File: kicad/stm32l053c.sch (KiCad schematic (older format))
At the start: 13 parts, among them P1 SWD, U1 STM32L053C8_LQFP48

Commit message: LCD footprint
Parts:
- added U1: LCD_KITCHEN_TIMER, symbol LCD_KITCHEN_TIMER
- gave numbers to parts that had none: 1
- renumbered C5 to C1, C7 to C2, C8 to C3, C6 to C5, C1 to C6, C2 to C7, R4 to R1, R1 to R2, U1 to U2
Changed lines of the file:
@@
 LIBS:valves
 LIBS:stm32
+LIBS:lcd_kitchen_timer
+LIBS:stm32l053c-cache
 EELAYER 25 0
 EELAYER END
@@
 $EndDescr
 $Comp
-L Earth #PWR17
+L Earth #PWR5
 U 1 1 58021BE1
 P 9650 1350
-F 0 "#PWR17" H 9650 1100 50  0001 C CNN
+F 0 "#PWR5" H 9650 1100 50  0001 C CNN
 F 1 "Earth" H 9650 1200 50  0001 C CNN
 F 2 "" H 9650 1350 50  0000 C CNN
@@
 $EndComp
 $Comp
-L VDD #PWR16
+L VDD #PWR2
 U 1 1 58021C2A
 P 9650 1050
-F 0 "#PWR16" H 9650 900 50  0001 C CNN
+F 0 "#PWR2" H 9650 900 50  0001 C CNN
 F 1 "VDD" H 9650 1200 50  0000 C CNN
 F 2 "" H 9650 1050 50  0000 C CNN
@@
 $EndComp
 $Comp
-L C C5
+L C C1
 U 1 1 58021E64
 P 9650 1200
-F 0 "C5" H 9675 1300 50  0000 L CNN
+F 0 "C1" H 9675 1300 50  0000 L CNN
 F 1 "100nF" H 9675 1100 50  0000 L CNN
 F 2 "Capacitors_SMD:C_0805_HandSoldering" H 9688 1050 50  0001 C CNN
@@
 $EndComp
 $Comp
-L GNDA #PWR12
+L GNDA #PWR15
 U 1 1 58021F75
 P 7050 6200
-F 0 "#PWR12" H 7050 5950 50  0001 C CNN
+F 0 "#PWR15" H 7050 5950 50  0001 C CNN
 F 1 "GNDA" H 7050 6050 50  0000 C CNN
 F 2 "" H 7050 6200 50  0000 C CNN
@@
 $EndComp
 $Comp
-L Earth #PWR15
+L Earth #PWR16
 U 1 1 58021F89
 P 7550 6200
-F 0 "#PWR15" H 7550 5950 50  0001 C CNN
+F 0 "#PWR16" H 7550 5950 50  0001 C CNN
 F 1 "Earth" H 7550 6050 50  0001 C CNN
 F 2 "" H 7550 6200 50  0000 C CNN
@@
 $EndComp
 $Comp
-L GNDA #PWR11
+L GNDA #PWR13
 U 1 1 58022154
 P 7050 5700
-F 0 "#PWR11" H 7050 5450 50  0001 C CNN
+F 0 "#PWR13" H 7050 5450 50  0001 C CNN
 F 1 "GNDA" H 7050 5550 50  0000 C CNN
 F 2 "" H 7050 5700 50  0000 C CNN
@@
 $EndComp
 $Comp
-L VDD #PWR13
+L VDD #PWR1
 U 1 1 5802295B
 P 7350 950
-F 0 "#PWR13" H 7350 800 50  0001 C CNN
+F 0 "#PWR1" H 7350 800 50  0001 C CNN
 F 1 "VDD" H 7350 1100 50  0000 C CNN
 F 2 "" H 7350 950 50  0000 C CNN
@@
 $EndComp
 $Comp
-L Earth #PWR10
+L Earth #PWR7
 U 1 1 5803310F
 P 6700 1700
-F 0 "#PWR10" H 6700 1450 50  0001 C CNN
+F 0 "#PWR7" H 6700 1450 50  0001 C CNN
 F 1 "Earth" H 6700 1550 50  0001 C CNN
 F 2 "" H 6700 1700 50  0000 C CNN
@@
 $EndComp
 $Comp
-L Earth #PWR6
+L Earth #PWR4
 U 1 1 580369A9
 P 2400 1350
-F 0 "#PWR6" H 2400 1100 50  0001 C CNN
+F 0 "#PWR4" H 2400 1100 50  0001 C CNN
 F 1 "Earth" H 2400 1200 50  0001 C CNN
 F 2 "" H 2400 1350 50  0000 C CNN
@@
 NRST
 $Comp
-L VDD #PWR4
+L VDD #PWR3
 U 1 1 5803734F
 P 1900 1150
-F 0 "#PWR4" H 1900 1000 50  0001 C CNN
+F 0 "#PWR3" H 1900 1000 50  0001 C CNN
 F 1 "VDD" H 1900 1300 50  0000 C CNN
 F 2 "" H 1900 1150 50  0000 C CNN
@@
 LCD_COM3
 $Comp
-L Earth #PWR19
+L Earth #PWR9
 U 1 1 58039244
 P 9650 2100
-F 0 "#PWR19" H 9650 1850 50  0001 C CNN
+F 0 "#PWR9" H 9650 1850 50  0001 C CNN
 F 1 "Earth" H 9650 1950 50  0001 C CNN
 F 2 "" H 9650 2100 50  0000 C CNN
@@
 $EndComp
 $Comp
-L VDD #PWR18
+L VDD #PWR8
 U 1 1 5803924A
 P 9650 1800
-F 0 "#PWR18" H 9650 1650 50  0001 C CNN
+F 0 "#PWR8" H 9650 1650 50  0001 C CNN
 F 1 "VDD" H 9650 1950 50  0000 C CNN
 F 2 "" H 9650 1800 50  0000 C CNN
@@
 $EndComp
 $Comp
-L C C6
+L C C5
 U 1 1 58039250
 P 9650 1950
-F 0 "C6" H 9675 2050 50  0000 L CNN
+F 0 "C5" H 9675 2050 50  0000 L CNN
 F 1 "10uF" H 9675 1850 50  0000 L CNN
 F 2 "Capacitors_SMD:C_0805_HandSoldering" H 9688 1800 50  0001 C CNN
@@
 $EndComp
 $Comp
-L C C7
+L C C2
 U 1 1 5803B990
 P 9950 1200
-F 0 "C7" H 9975 1300 50  0000 L CNN
+F 0 "C2" H 9975 1300 50  0000 L CNN
 F 1 "100nF" H 9975 1100 50  0000 L CNN
 F 2 "Capacitors_SMD:C_0805_HandSoldering" H 9988 1050 50  0001 C CNN
@@
 $EndComp
 $Comp
-L C C8
+L C C3
 U 1 1 5803BA4A
 P 10700 1200
-F 0 "C8" H 10725 1300 50  0000 L CNN
+F 0 "C3" H 10725 1300 50  0000 L CNN
 F 1 "100nF" H 10725 1100 50  0000 L CNN
 F 2 "Capacitors_SMD:C_0805_HandSoldering" H 10738 1050 50  0001 C CNN
@@
 $EndComp
 $Comp
-L Earth #PWR20
+L Earth #PWR6
 U 1 1 5803BDC8
 P 10700 1350
-F 0 "#PWR20" H 10700 1100 50  0001 C CNN
+F 0 "#PWR6" H 10700 1100 50  0001 C CNN
 F 1 "Earth" H 10700 1200 50  0001 C CNN
 F 2 "" H 10700 1350 50  0000 C CNN
@@
 VDD
 $Comp
-L STM32L053C8_LQFP48 U1
+L STM32L053C8_LQFP48 U2
 U 1 1 580631B3
 P 7350 4000
-F 0 "U1" H 8000 6000 60  0000 C CNN
+F 0 "U2" H 8000 6000 60  0000 C CNN
 F 1 "STM32L053C8_LQFP48" H 7450 4000 60  0000 C CNN
 F 2 "Housings_QFP:LQFP-48_7x7mm_Pitch0.5mm" H 7150 2100 60  0001 C CNN
@@
 $EndComp
 $Comp
-L R R1
+L R R2
 U 1 1 5806575A
 P 8450 5150
-F 0 "R1" V 8530 5150 50  0000 C CNN
+F 0 "R2" V 8530 5150 50  0000 C CNN
 F 1 "10K" V 8450 5150 50  0000 C CNN
 F 2 "Resistors_SMD:R_0805_HandSoldering" V 8380 5150 50  0001 C CNN
@@
 $EndComp
 $Comp
-L Earth #PWR7
+L Earth #PWR11
 U 1 1 58065816
 P 8450 5300
-F 0 "#PWR7" H 8450 5050 50  0001 C CNN
+F 0 "#PWR11" H 8450 5050 50  0001 C CNN
 F 1 "Earth" H 8450 5150 50  0001 C CNN
 F 2 "" H 8450 5300 50  0000 C CNN
@@
 Connection ~ 7350 5550
 Wire Wire Line
-	7350 950  7350 1900
+	7350 950  7350 1150
+Wire Wire Line
+	7350 1150 7350 1900
 Wire Wire Line
 	7450 1150 7450 1900
@@
 	7200 1150 7200 1900
 Wire Wire Line
-	7200 1150 7800 1150
+	7200 1150 7350 1150
+Wire Wire Line
+	7350 1150 7450 1150
+Wire Wire Line
+	7450 1150 7800 1150
 Connection ~ 7350 1150
 Wire Wire Line
@@
 	9950 1350 9650 1350
 $Comp
-L C C2
+L C C7
 U 1 1 5806648B
 P 5650 5300
-F 0 "C2" H 5675 5400 50  0000 L CNN
+F 0 "C7" H 5675 5400 50  0000 L CNN
 F 1 "20pF" H 5675 5200 50  0000 L CNN
 F 2 "Capacitors_SMD:C_0805_HandSoldering" H 5688 5150 50  0001 C CNN
@@
 $EndComp
 $Comp
-L C C1
+L C C6
 U 1 1 580665CF
 P 5350 5300
-F 0 "C1" H 5375 5400 50  0000 L CNN
+F 0 "C6" H 5375 5400 50  0000 L CNN
 F 1 "20pF" H 5375 5200 50  0000 L CNN
 F 2 "Capacitors_SMD:C_0805_HandSoldering" H 5388 5150 50  0001 C CNN
@@
 $EndComp
 $Comp
-L Earth #PWR8
+L Earth #PWR12
 U 1 1 5806680D
 P 5500 5600
-F 0 "#PWR8" H 5500 5350 50  0001 C CNN
+F 0 "#PWR12" H 5500 5350 50  0001 C CNN
 F 1 "Earth" H 5500 5450 50  0001 C CNN
 F 2 "" H 5500 5600 50  0000 C CNN
@@
 $EndComp
 $Comp
-L R R4
+L R R1
 U 1 1 580770D7
 P 9600 4200
-F 0 "R4" V 9680 4200 50  0000 C CNN
+F 0 "R1" V 9680 4200 50  0000 C CNN
 F 1 "820" V 9600 4200 50  0000 C CNN
 F 2 "Resistors_SMD:R_0805_HandSoldering" V 9530 4200 50  0001 C CNN
@@
 $EndComp
 $Comp
-L Earth #PWR5
+L Earth #PWR10
 U 1 1 58077163
 P 10250 4300
-F 0 "#PWR5" H 10250 4050 50  0001 C CNN
+F 0 "#PWR10" H 10250 4050 50  0001 C CNN
 F 1 "Earth" H 10250 4150 50  0001 C CNN
 F 2 "" H 10250 4300 50  0000 C CNN
@@
 Wire Wire Line
 	10250 4200 10150 4200
-Text Label 9250 4200 0    60   ~ 0
-PA5
 Wire Wire Line
 	9250 4200 9450 4200
@@
 	8450 2500 9000 2500
 Wire Wire Line
-	7350 5550 7550 5550
+	7350 5550 7450 5550
+Wire Wire Line
+	7450 5550 7550 5550
 NoConn ~ 6500 4900
 NoConn ~ 6500 5000
@@
 NoConn ~ 6500 3700
 $Comp
-L Crystal Y?
+L Crystal Y1
 U 1 1 584DF533
 P 5500 4950
-F 0 "Y?" H 5500 5100 50  0000 C CNN
+F 0 "Y1" H 5500 5100 50  0000 C CNN
 F 1 "Crystal" H 5500 4800 50  0000 C CNN
 F 2 "" H 5500 4950 50  0000 C CNN
@@
 	5350 4700 6500 4700
 Wire Wire Line
-	5350 4700 5350 5150
+	5350 4700 5350 4950
+Wire Wire Line
+	5350 4950 5350 5150
 Connection ~ 5350 4950
 Wire Wire Line
 	5650 4800 6500 4800
 Wire Wire Line
-	5650 4800 5650 5150
+	5650 4800 5650 4950
+Wire Wire Line
+	5650 4950 5650 5150
 Connection ~ 5650 4950
 Wire Wire Line
 	5650 5600 5650 5450
 Wire Wire Line
-	5350 5600 5650 5600
+	5350 5600 5500 5600
+Wire Wire Line
+	5500 5600 5650 5600
 Wire Wire Line
 	5350 5450 5350 5600
 Connection ~ 5500 5600
 NoConn ~ 6500 4600
+$Comp
+L LCD_KITCHEN_TIMER U1
+U 1 1 584EB0DA
+P 2900 3600
+F 0 "U1" H 2900 3800 60  0000 C CNN
+F 1 "LCD_KITCHEN_TIMER" H 2900 3600 60  0000 C CNN
+F 2 "" H 2900 3600 60  0000 C CNN
+F 3 "" H 2900 3600 60  0000 C CNN
+	1    2900 3600
+	1    0    0    -1
+$EndComp
+Text GLabel 9250 4200 0    60   Input ~ 0
+PA5
 $EndSCHEMATC

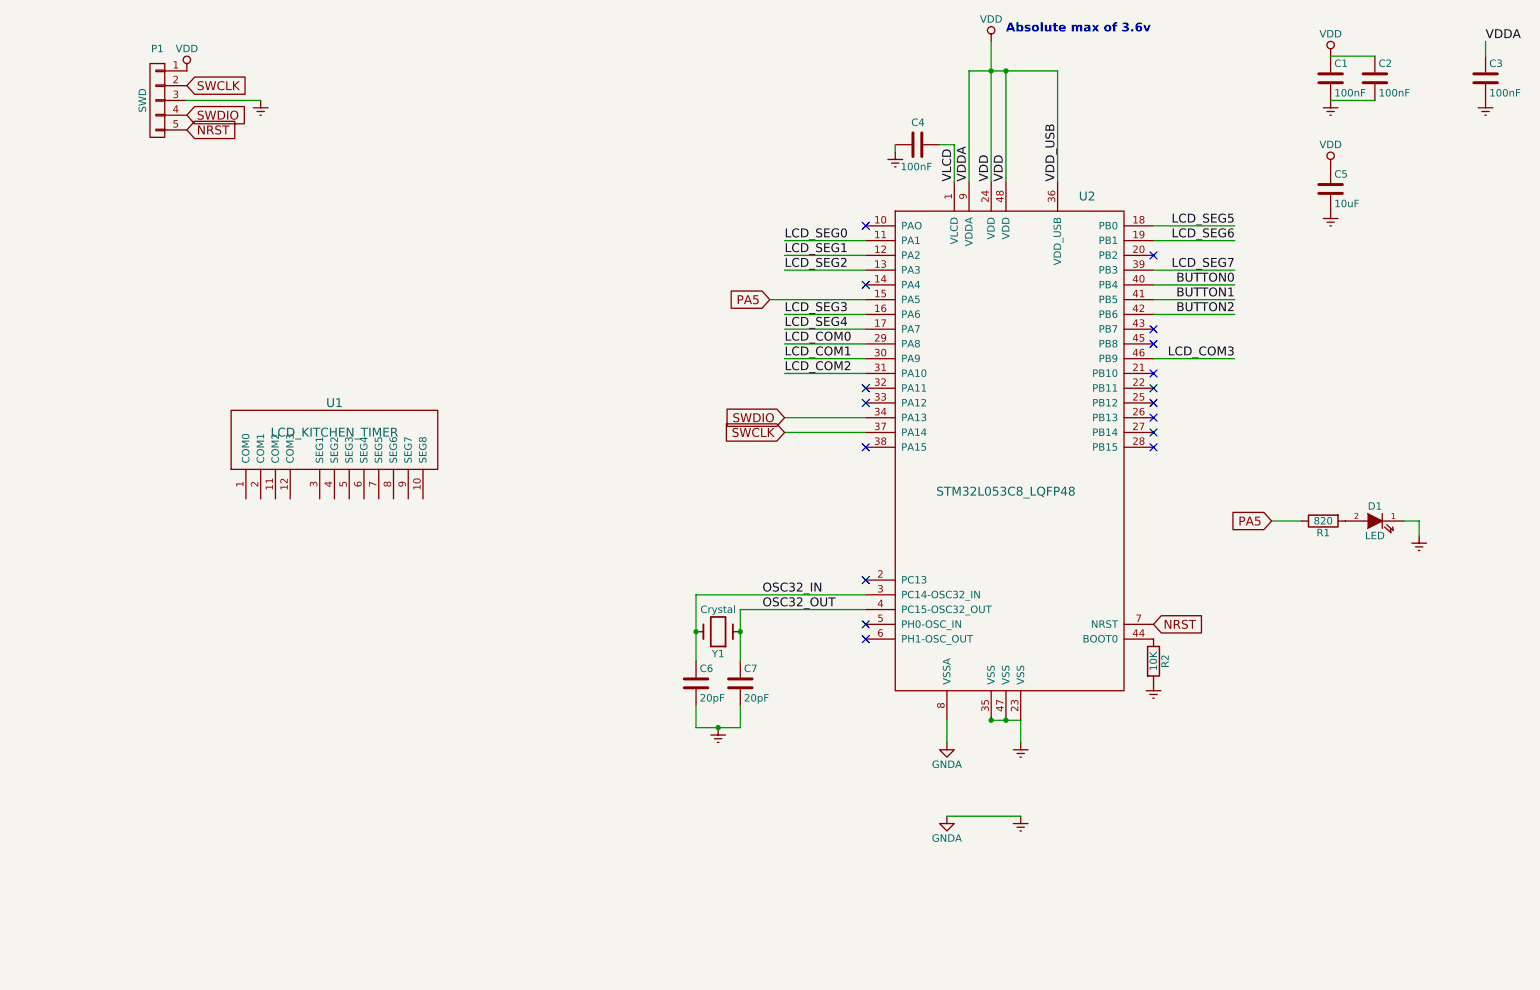
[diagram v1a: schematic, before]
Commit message: LCD connections
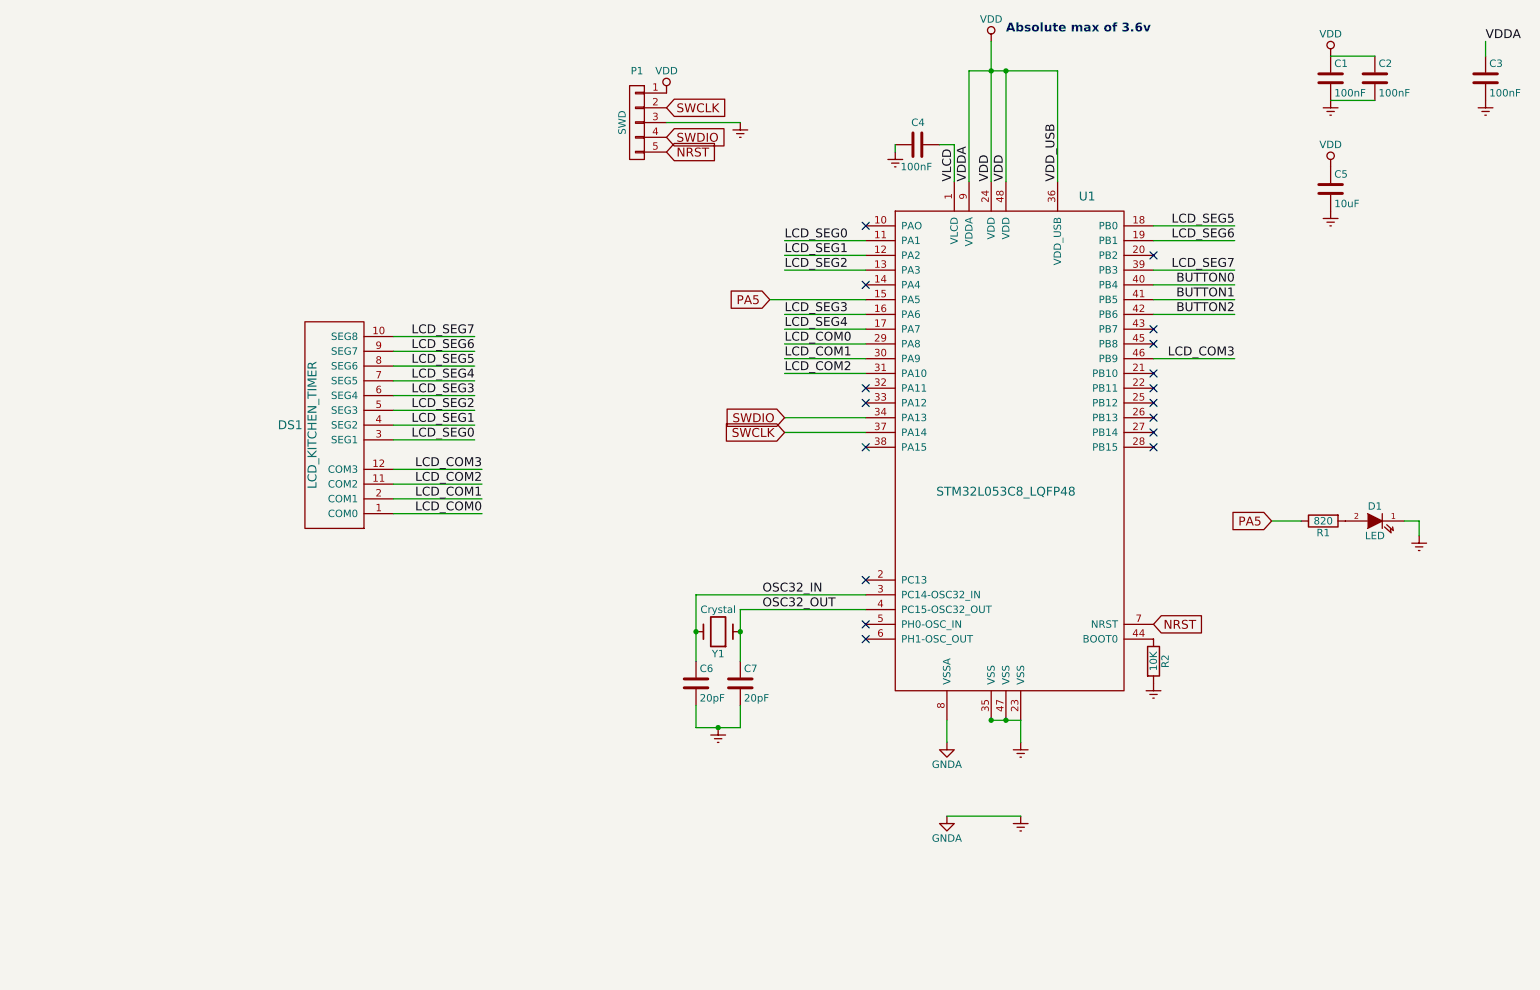
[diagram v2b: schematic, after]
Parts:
- removed U1: LCD_KITCHEN_TIMER, symbol LCD_KITCHEN_TIMER
- added DS1: LCD_KITCHEN_TIMER, symbol LCD_KITCHEN_TIMER
- renumbered U2 to U1
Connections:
- net LCD_COM0: now also DS1.1 (COM0)
- net LCD_COM1: now also DS1.2 (COM1)
- net LCD_COM2: now also DS1.11 (COM2)
- net LCD_COM3: now also DS1.12 (COM3)
- net LCD_SEG0: now also DS1.3 (SEG1)
- net LCD_SEG1: now also DS1.4 (SEG2)
- net LCD_SEG2: now also DS1.5 (SEG3)
- net LCD_SEG3: now also DS1.6 (SEG4)
- net LCD_SEG4: now also DS1.7 (SEG5)
- net LCD_SEG5: now also DS1.8 (SEG6)
- net LCD_SEG6: now also DS1.9 (SEG7)
- net LCD_SEG7: now also DS1.10 (SEG8)
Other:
- moved on the sheet: P1
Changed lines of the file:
@@
 $EndDescr
 $Comp
-L Earth #PWR5
+L Earth #PWR4
 U 1 1 58021BE1
 P 9650 1350
-F 0 "#PWR5" H 9650 1100 50  0001 C CNN
+F 0 "#PWR4" H 9650 1100 50  0001 C CNN
 F 1 "Earth" H 9650 1200 50  0001 C CNN
 F 2 "" H 9650 1350 50  0000 C CNN
@@
 L CONN_01X05 P1
 U 1 1 58036840
-P 1700 1350
-F 0 "P1" H 1700 1700 50  0000 C CNN
-F 1 "SWD" V 1800 1350 50  0000 C CNN
-F 2 "Pin_Headers:Pin_Header_Straight_1x06" H 1700 1350 50  0001 C CNN
-F 3 "" H 1700 1350 50  0000 C CNN
-	1    1700 1350
+P 4950 1500
+F 0 "P1" H 4950 1850 50  0000 C CNN
+F 1 "SWD" V 5050 1500 50  0000 C CNN
+F 2 "Pin_Headers:Pin_Header_Straight_1x06" H 4950 1500 50  0001 C CNN
+F 3 "" H 4950 1500 50  0000 C CNN
+	1    4950 1500
 	-1   0    0    -1
 $EndComp
 $Comp
-L Earth #PWR4
+L Earth #PWR6
 U 1 1 580369A9
-P 2400 1350
-F 0 "#PWR4" H 2400 1100 50  0001 C CNN
-F 1 "Earth" H 2400 1200 50  0001 C CNN
-F 2 "" H 2400 1350 50  0000 C CNN
-F 3 "" H 2400 1350 50  0000 C CNN
-	1    2400 1350
-	1    0    0    -1
-$EndComp
-Text GLabel 1900 1250 2    60   Input ~ 0
+P 5650 1500
+F 0 "#PWR6" H 5650 1250 50  0001 C CNN
+F 1 "Earth" H 5650 1350 50  0001 C CNN
+F 2 "" H 5650 1500 50  0000 C CNN
+F 3 "" H 5650 1500 50  0000 C CNN
+	1    5650 1500
+	1    0    0    -1
+$EndComp
+Text GLabel 5150 1400 2    60   Input ~ 0
 SWCLK
-Text GLabel 1900 1450 2    60   Input ~ 0
+Text GLabel 5150 1600 2    60   Input ~ 0
 SWDIO
-Text GLabel 1900 1550 2    60   Input ~ 0
+Text GLabel 5150 1700 2    60   Input ~ 0
 NRST
 $Comp
 L VDD #PWR3
 U 1 1 5803734F
-P 1900 1150
-F 0 "#PWR3" H 1900 1000 50  0001 C CNN
-F 1 "VDD" H 1900 1300 50  0000 C CNN
-F 2 "" H 1900 1150 50  0000 C CNN
-F 3 "" H 1900 1150 50  0000 C CNN
-	1    1900 1150
+P 5150 1300
+F 0 "#PWR3" H 5150 1150 50  0001 C CNN
+F 1 "VDD" H 5150 1450 50  0000 C CNN
+F 2 "" H 5150 1300 50  0000 C CNN
+F 3 "" H 5150 1300 50  0000 C CNN
+	1    5150 1300
 	1    0    0    -1
 $EndComp
@@
 $EndComp
 $Comp
-L Earth #PWR6
+L Earth #PWR5
 U 1 1 5803BDC8
 P 10700 1350
-F 0 "#PWR6" H 10700 1100 50  0001 C CNN
+F 0 "#PWR5" H 10700 1100 50  0001 C CNN
 F 1 "Earth" H 10700 1200 50  0001 C CNN
 F 2 "" H 10700 1350 50  0000 C CNN
@@
 VDD
 $Comp
-L STM32L053C8_LQFP48 U2
+L STM32L053C8_LQFP48 U1
 U 1 1 580631B3
 P 7350 4000
-F 0 "U2" H 8000 6000 60  0000 C CNN
+F 0 "U1" H 8000 6000 60  0000 C CNN
 F 1 "STM32L053C8_LQFP48" H 7450 4000 60  0000 C CNN
 F 2 "Housings_QFP:LQFP-48_7x7mm_Pitch0.5mm" H 7150 2100 60  0001 C CNN
@@
 Connection ~ 7350 5550
 Wire Wire Line
-	7350 950  7350 1150
-Wire Wire Line
-	7350 1150 7350 1900
+	7350 950  7350 1900
 Wire Wire Line
 	7450 1150 7450 1900
@@
 	7200 1150 7200 1900
 Wire Wire Line
-	7200 1150 7350 1150
-Wire Wire Line
-	7350 1150 7450 1150
-Wire Wire Line
-	7450 1150 7800 1150
+	7200 1150 7800 1150
 Connection ~ 7350 1150
 Wire Wire Line
@@
 	5950 3600 6500 3600
 Wire Wire Line
-	2400 1350 1900 1350
+	5650 1500 5150 1500
 Wire Wire Line
 	7550 6200 7050 6200
@@
 	8450 2500 9000 2500
 Wire Wire Line
-	7350 5550 7450 5550
-Wire Wire Line
-	7450 5550 7550 5550
+	7350 5550 7550 5550
 NoConn ~ 6500 4900
 NoConn ~ 6500 5000
@@
 	5350 4700 6500 4700
 Wire Wire Line
-	5350 4700 5350 4950
-Wire Wire Line
-	5350 4950 5350 5150
+	5350 4700 5350 5150
 Connection ~ 5350 4950
 Wire Wire Line
 	5650 4800 6500 4800
 Wire Wire Line
-	5650 4800 5650 4950
-Wire Wire Line
-	5650 4950 5650 5150
+	5650 4800 5650 5150
 Connection ~ 5650 4950
 Wire Wire Line
 	5650 5600 5650 5450
 Wire Wire Line
-	5350 5600 5500 5600
-Wire Wire Line
-	5500 5600 5650 5600
+	5350 5600 5650 5600
 Wire Wire Line
 	5350 5450 5350 5600
 Connection ~ 5500 5600
 NoConn ~ 6500 4600
-$Comp
-L LCD_KITCHEN_TIMER U1
-U 1 1 584EB0DA
-P 2900 3600
-F 0 "U1" H 2900 3800 60  0000 C CNN
-F 1 "LCD_KITCHEN_TIMER" H 2900 3600 60  0000 C CNN
-F 2 "" H 2900 3600 60  0000 C CNN
-F 3 "" H 2900 3600 60  0000 C CNN
-	1    2900 3600
-	1    0    0    -1
-$EndComp
 Text GLabel 9250 4200 0    60   Input ~ 0
 PA5
+Text Label 3900 4150 2    60   ~ 0
+LCD_COM0
+Text Label 3900 4050 2    60   ~ 0
+LCD_COM1
+Text Label 3900 3950 2    60   ~ 0
+LCD_COM2
+Text Label 3850 3650 2    60   ~ 0
+LCD_SEG0
+Text Label 3850 3550 2    60   ~ 0
+LCD_SEG1
+Text Label 3850 3450 2    60   ~ 0
+LCD_SEG2
+Text Label 3850 3350 2    60   ~ 0
+LCD_SEG3
+Text Label 3850 3250 2    60   ~ 0
+LCD_SEG4
+Text Label 3850 3150 2    60   ~ 0
+LCD_SEG5
+Text Label 3850 3050 2    60   ~ 0
+LCD_SEG6
+Text Label 3850 2950 2    60   ~ 0
+LCD_SEG7
+Text Label 3900 3850 2    60   ~ 0
+LCD_COM3
+Wire Wire Line
+	3900 3850 3300 3850
+Wire Wire Line
+	3300 3950 3900 3950
+Wire Wire Line
+	3300 4050 3900 4050
+Wire Wire Line
+	3300 4150 3900 4150
+Wire Wire Line
+	3300 3650 3850 3650
+Wire Wire Line
+	3850 3550 3300 3550
+Wire Wire Line
+	3300 3450 3850 3450
+Wire Wire Line
+	3850 3350 3300 3350
+Wire Wire Line
+	3300 3250 3850 3250
+Wire Wire Line
+	3300 3150 3850 3150
+Wire Wire Line
+	3850 3050 3300 3050
+Wire Wire Line
+	3300 2950 3850 2950
+$Comp
+L LCD_KITCHEN_TIMER DS1
+U 1 1 584F1C3C
+P 2850 3550
+F 0 "DS1" V 2850 3800 60  0000 C CNN
+F 1 "LCD_KITCHEN_TIMER" H 2850 3650 60  0000 C CNN
+F 2 "" H 2850 3550 60  0000 C CNN
+F 3 "" H 2850 3550 60  0000 C CNN
+	1    2850 3550
+	0    -1   -1   0
+$EndComp
 $EndSCHEMATC

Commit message: Power supply
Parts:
- removed C5: 10uF, Capacitors_SMD:C_0805_HandSoldering, symbol C
- added C8, C9: 10uF, Capacitors_SMD:C_0805_HandSoldering, symbol C
- added L1: INDUCTOR, symbol INDUCTOR
- added U2: TLV61225, symbol TLV61225
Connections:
- net Earth: now also C8.2, C9.2, U2.3 (GND)
- net VDD: now also C8.1, U2.2 (FB), U2.4 (VOUT)
- new net: L1.2, U2.5 (L)
- new net +BATT: C9.1, L1.1, U2.1 (VIN), U2.6 (EN)
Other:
- note added: "1V5"
- note added: "3V3"
- note removed: "Absolute max of 3.6v"
- moved on the sheet: C1, C2, C3, C4, C6, C7, D1, DS1, P1, R1, R2, U1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
